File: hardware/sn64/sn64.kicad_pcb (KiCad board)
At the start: 6 copper layers, 101.8 x 76.5 mm, 410 parts, among them J1 N64_Cartridge_Edge_50, J101 DX07S016JA3R1500, J102 JTAG_SERVICE, J2 SN64_Socket_Joint_2x40, Q201 2N7002, Q301 BSS138BK, Q302 BSS138BK, Q303 BSS138BK, Q304 BSS138BK, Q305 BSS138BK, Q306 BSS138BK, Q307 BSS138BK, Q308 BSS138BK, U101 USBLC6-2SC6, U102 USBLC6-2SC6, U103 AP2112K-3.3TRG1, U104 FT232HL (rev C), U105 SN74AXC4T774PWR, U106 93AA56BT-I/OT (DNP), U201 SN74LVC4245APWR, U202 SN74LVC4245APWR, U203 SN74LVC4245APWR, U204 SN74LVC4245APWR, U205 SN74LVC4245APWR, U206 SN74LVC4245APWR, U207 SN74LVC4245APWR, U209 SN74LVC244APWR, U210 SN74LVC1G07DBVR, U211 SN74LVC1G07DBVR, U212 SN74LVC1G07DBVR, U213 SN74LVC1G06DBVR, U214 SN74LVC1G06DBVR, U215 SN74LVC1T45DBVR, U216 SN74LVC1T45DBVR, U301 TUSB320IRWBR, U302 TPS259470LRPWR, U303 TPS259470LRPWR, U304 TPS63070RNMR, U305 TLV62569DBVR, U306 TLV62569DBVR, U307 TLV62569DBVR, U308 TPS22918DBVR, U309 TPS259470LRPWR, U310 TPS3700DDCR, U311 TPS3700DDCR, U312 TPS3700DDCR, U313 TPS3700DDCR, U314 TPS3700DDCR, U315 TPS3700DDCR, U316 TPS3808G01DBVR, U317 TMP302ADRLR, U401 LFE5U-85F-6BG381C, U402 SN74CB3Q3384APWR, U403 SN74CB3Q3384APWR, U404 SN74CB3Q3384APWR, U405 W25Q128JVSIQ, U406 SN74LVC1G14DBVR, U407 SN74LVC1G07DBVR, U701 Si5351A-B-GTR, U703 PCM1808PWR, X701 25MHz CJO05-250003320B30, X702 12.288MHz CJO05-122883320B30, Y101 ABM3B-12.000MHZ-10-1-U-T, Y701 25MHz 10pF

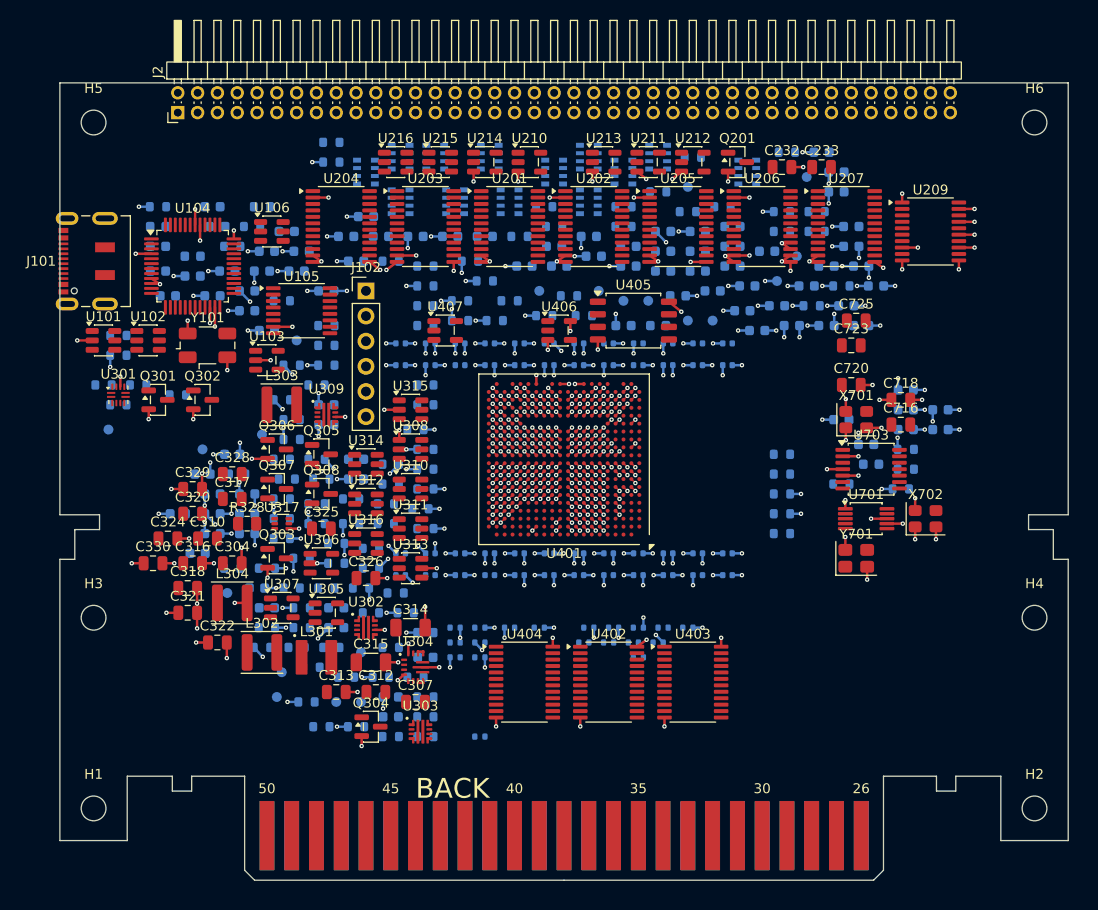
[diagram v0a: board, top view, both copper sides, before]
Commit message: PCB: first routed draft of the main board (KiCadRoutingTools run 2 + plane vias)
Tracked board: FPGA at 180 degrees, 240 dog-bone fan-out vias, GND/3V3
planes and the 1V1 island, signals routed by KiCadRoutingTools (Rust A*,
pinned to the board's fab floors), 157 plane vias, outer GND pours. DRC has
no shorts, crossings, clearance or hole errors; open: 75 signal/power nets
(95 connections, mostly the translator row) and 219 plane pads, listed in
validation/pcb-open-connections.json. Renders updated.

Tools: add_plane_vias.py (layer-aware stubs, edge and keep-out checks),
finish_route.py --no-import, fab-pcbway.txt; hole-to-copper 0.2 mm (PCBWay
8 mil). Notes on the three routers tried, the PCBWay capability check and
the KiCad 10 python pitfalls in docs/design/pcb-routing.md and the work log.

Co-Authored-By: Claude Fable 5.1 <noreply@anthropic.com>
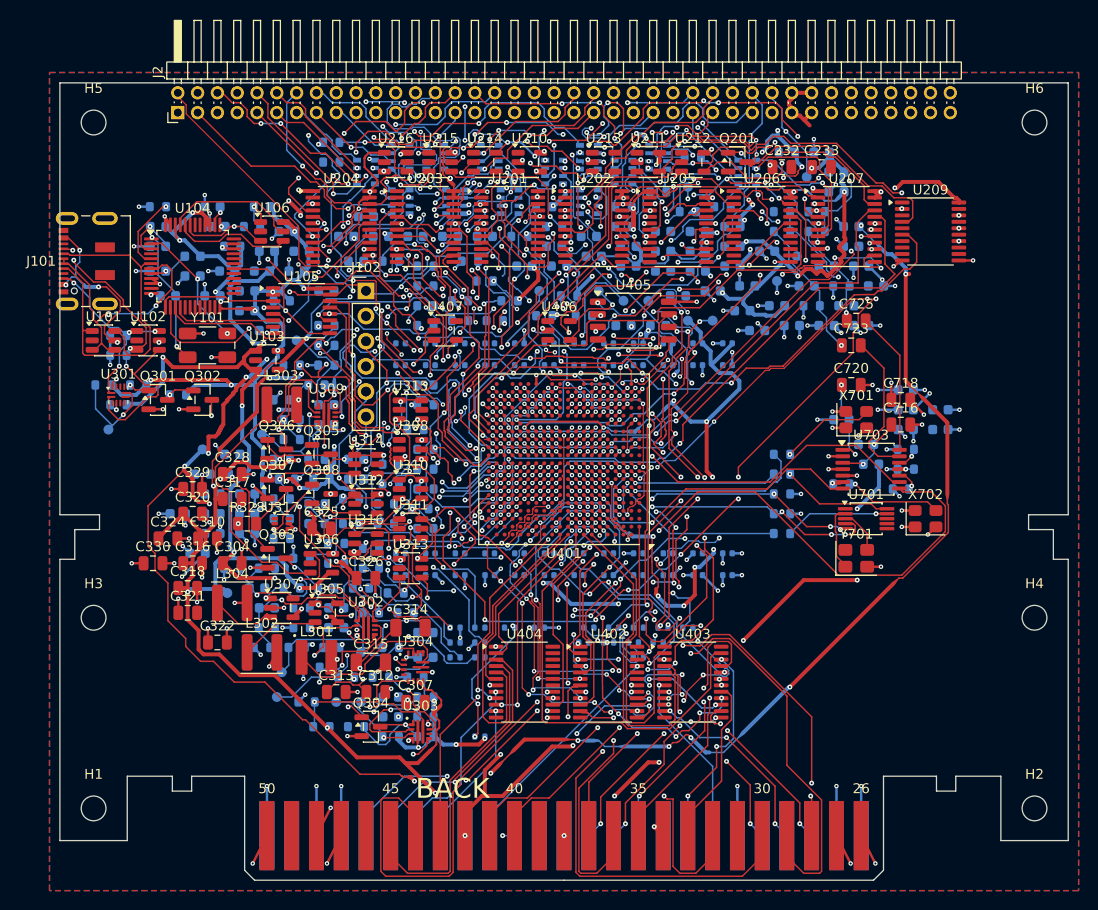
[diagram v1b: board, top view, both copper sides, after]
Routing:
- net /SNES_5V_CART: track 0.00 -> 354.6 mm, vias 0 -> 46
- net /INTERFACE_3V3: track 0.00 -> 252.7 mm, vias 0 -> 43
- net /5V_PRE: track 0.00 -> 225.5 mm, vias 0 -> 20
- net /USB_3V3: track 0.00 -> 122.7 mm, vias 0 -> 17
- net /SNES_EXPAND: track 0.00 -> 117.9 mm, vias 0 -> 10
- net /FPGA/FPGA_VCCAUX: track 2.26 -> 112.7 mm, vias 4 -> 17
- net /USB_VBUS: track 0.00 -> 103.5 mm, vias 0 -> 12
- net /FPGA/n64_sw_oe_n: track 0.00 -> 101.3 mm, vias 0 -> 9
- net /fpga_rails_ok: track 0.00 -> 101.0 mm, vias 0 -> 14
- net /GND: track 317.0 -> 225.3 mm, vias 322 -> 210
- net /cart_data2: track 0.57 -> 86.2 mm, vias 1 -> 11
- net /efuse_fault_n: track 0.57 -> 83.4 mm, vias 1 -> 8
- net /SNES cartridge interface/CTL_OE_N_5V: track 0.00 -> 75.5 mm, vias 0 -> 11
- net /jtag_tck: track 0.57 -> 75.5 mm, vias 1 -> 11
- net /cart_pa2: track 0.57 -> 73.4 mm, vias 1 -> 6
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- added copper zone on B.Cu, net /GND
- added copper zone on F.Cu, net /GND
